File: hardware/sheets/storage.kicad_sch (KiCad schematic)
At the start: 23 parts, among them J1 Conn_02x20_Odd_Even, J2 Conn_02x25_Odd_Even, Q1 2N7002, U1 74HC04, U10 74LVC573A, U11 74HC138, U3 74HC08, U4 74HC32, U6 74HC138, U7 74HC138, U8 74LVC245A, U9 74LVC573A

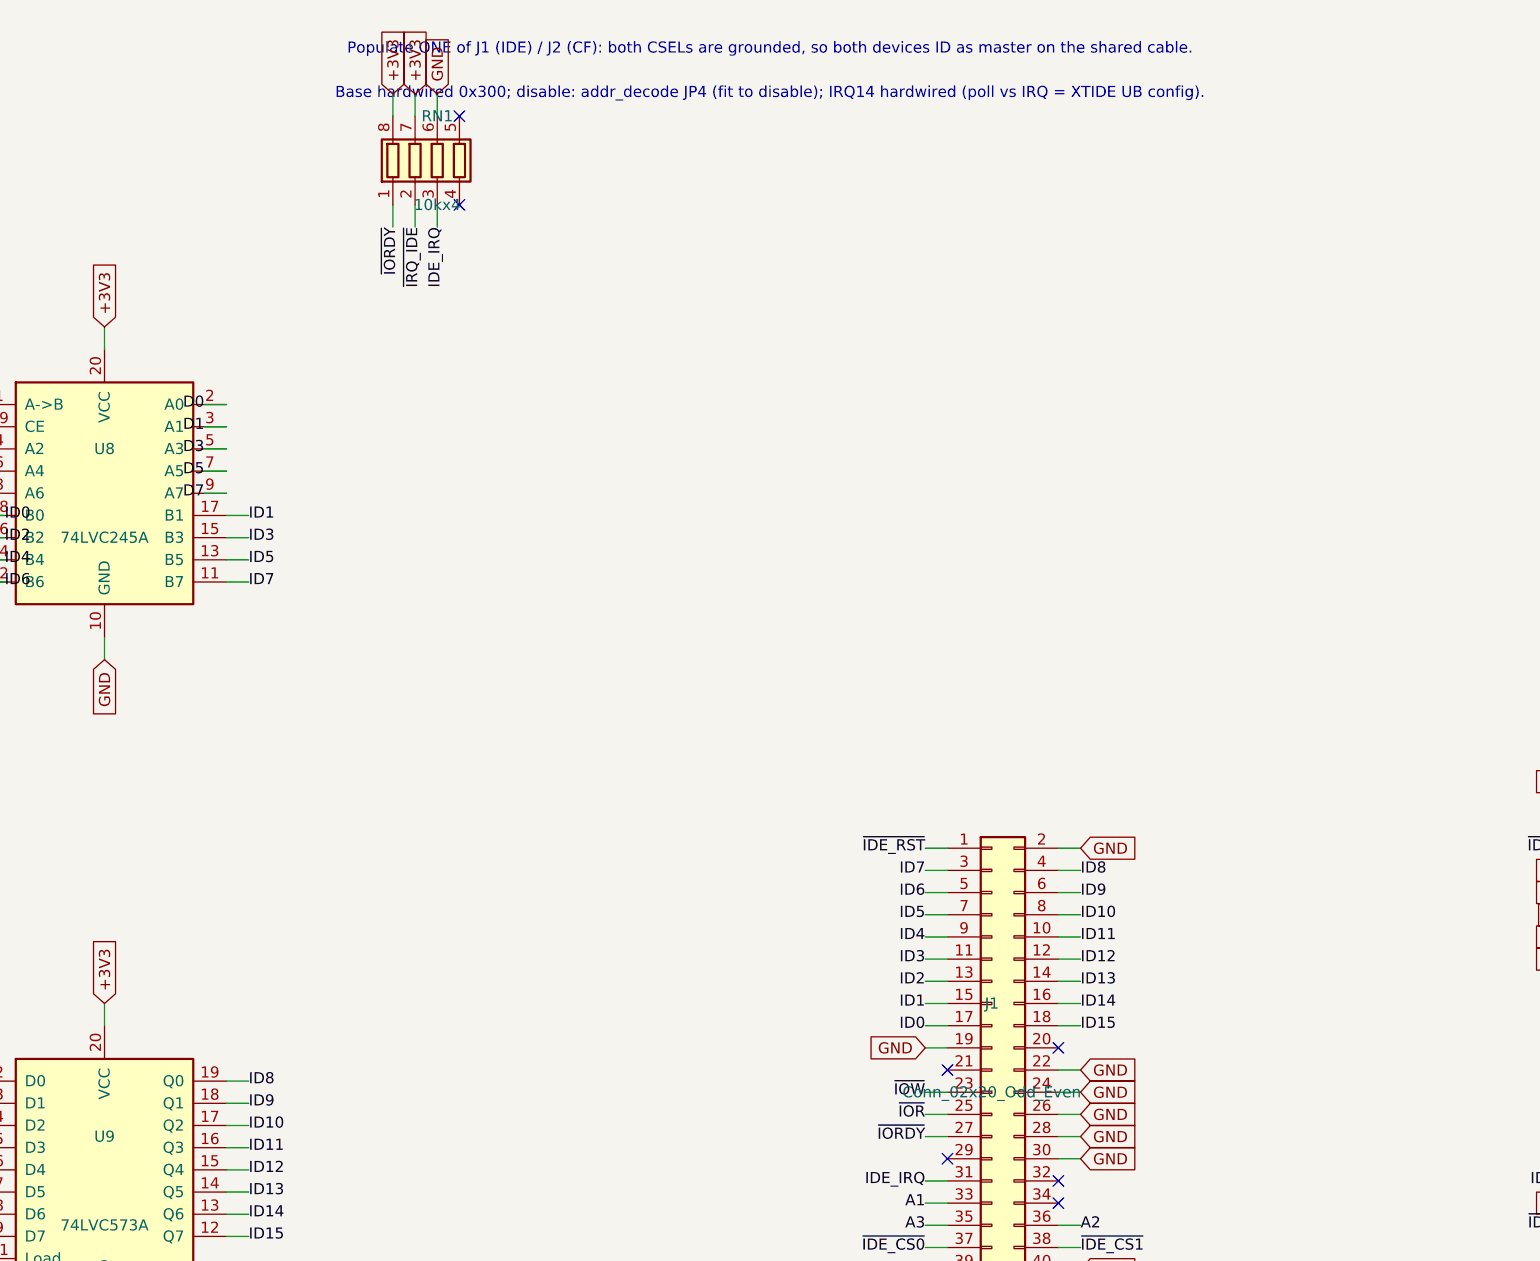
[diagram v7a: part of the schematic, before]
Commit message: Expansion port: 50-pin header, port DMA channel, dev cards deleted
Two waves of the 2026-07-14/15 expansion-port rework (the first was
uncommitted): the IRQ-scan collapse to one '165 + '32 OR rank with
ISA-card DMA removed outright, then the port redesign that brings one
DMA channel back:

- isa_conn: 60-pin (2x30, PicoGUS-standard layout) -> 50-pin (2x25,
  project-private pinout; 50-way IDC is far easier to source). OSC and
  ~REFRESH dropped to fit (no on-board consumer / no DRAM refresh; the
  planned ISA backplane board re-creates both for period cards).
- Port DMA: EXT_DRQ rides the sidecar inbound '244 + U12 '165 spare D6
  lane (zero GPIO); ~EXT_DACK = GPIO47 (freed by ~REFRESH) out through
  the strobe '244. Separate nets from the internal PicoGUS pair, so a
  port card never sees the on-board acknowledge.
- DRQ1/~DACK1 renamed DRQ/~DACK (ch2/3 long retired); DRQ2/3 +
  ~DACK2/3 removed from the mxbus contract.
- card_video + card_isatest deleted (sheets, hardware/cards/,
  build_cards()); superseded by the backplane plan. History has them.
- Connector parts: IDE header -> shrouded 2x20 IDC box (C9138, keypin
  20 NC'd); expansion port -> 90-degree 2x25 female socket (C21262364);
  addr_decode's five disable jumpers folded into ONE fixed 2x5 block
  JP1 (C492422), positions JP1.1-JP1.5 = COM1/COM2/LPT/IDE/VID.

ERC 0/0, check_parts 0 problems; docs/notes updated throughout.

Co-Authored-By: Claude Fable 5 <noreply@anthropic.com>
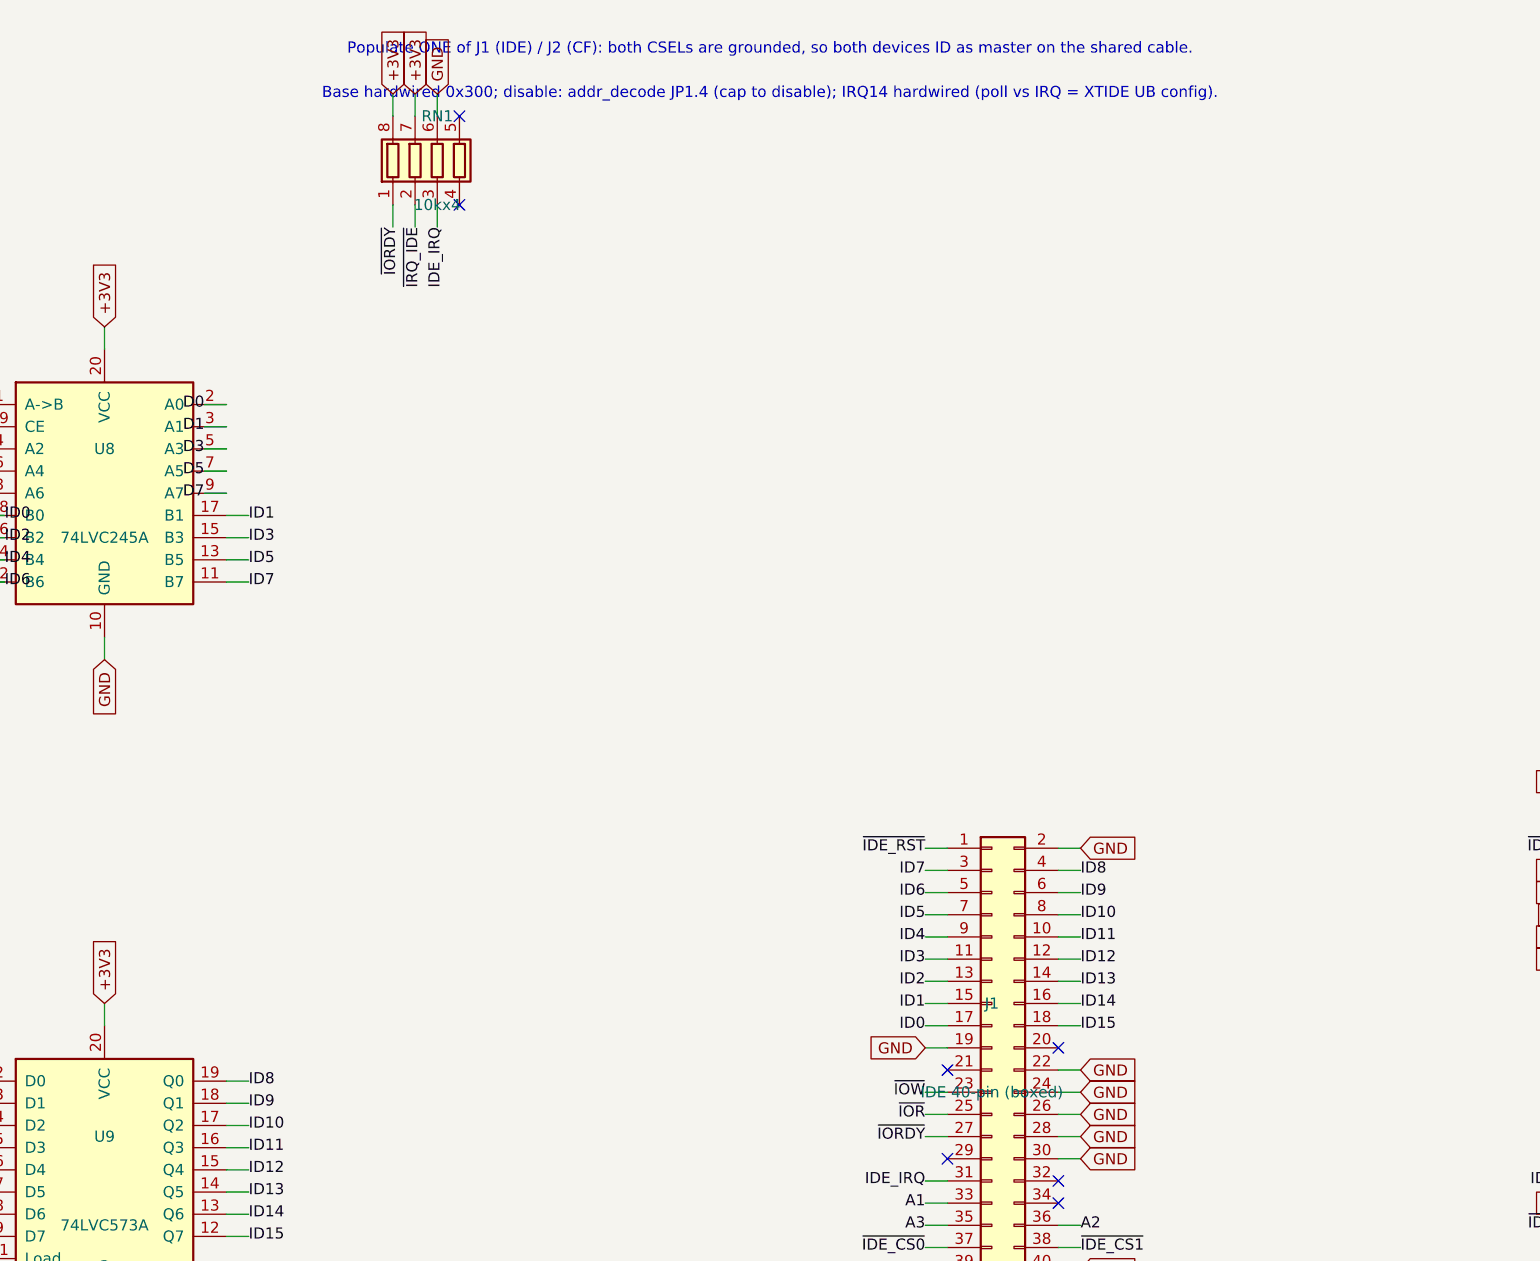
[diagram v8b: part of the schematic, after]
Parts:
- J1: value Conn_02x20_Odd_Even -> IDE 40-pin (boxed); footprint Connector_PinHeader_2.54mm:PinHeader_2x20_P2.54mm_Vertical -> Connector_IDC:IDC-Header_2x20_P2.54mm_Vertical; LCSC Part Num C2333 -> C9138
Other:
- note added: "Base hardwired 0x300; disable: addr_decode JP1.4 (cap to disable); IRQ14 hardwired (poll vs IRQ = XTIDE UB config)."
- note removed: "Base hardwired 0x300; disable: addr_decode JP4 (fit to disable); IRQ14 hardwired (poll vs IRQ = XTIDE UB config)."
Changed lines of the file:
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@@
 		)
 	)
-	(text "Base hardwired 0x300; disable: addr_decode JP4 (fit to disable); IRQ14 hardwired (poll vs IRQ = XTIDE UB config)."
+	(text "Base hardwired 0x300; disable: addr_decode JP1.4 (cap to disable); IRQ14 hardwired (poll vs IRQ = XTIDE UB config)."
 		(at 266.7 17.78 0)
 		(effects
@@
 		(instances
 			(project "mini-xt"
-				(path "/26736c46-8b40-5460-874f-03596d17270c/972bbf88-a469-5cda-af99-5a47d228ddba"
+				(path "/26736c46-8b40-5460-874f-03596d17270c/cea63665-b003-57d2-b8d8-5d97642a4726"
 					(reference "U801")
 					(unit 1)
@@
 		(instances
 			(project "mini-xt"
-				(path "/26736c46-8b40-5460-874f-03596d17270c/972bbf88-a469-5cda-af99-5a47d228ddba"
+				(path "/26736c46-8b40-5460-874f-03596d17270c/cea63665-b003-57d2-b8d8-5d97642a4726"
 					(reference "U803")
 					(unit 1)
@@
 		(instances
 			(project "mini-xt"
-				(path "/26736c46-8b40-5460-874f-03596d17270c/972bbf88-a469-5cda-af99-5a47d228ddba"
+				(path "/26736c46-8b40-5460-874f-03596d17270c/cea63665-b003-57d2-b8d8-5d97642a4726"
 					(reference "U804")
 					(unit 1)
@@
 		(instances
 			(project "mini-xt"
-				(path "/26736c46-8b40-5460-874f-03596d17270c/972bbf88-a469-5cda-af99-5a47d228ddba"
+				(path "/26736c46-8b40-5460-874f-03596d17270c/cea63665-b003-57d2-b8d8-5d97642a4726"
 					(reference "Q801")
 					(unit 1)
@@
 		(instances
 			(project "mini-xt"
-				(path "/26736c46-8b40-5460-874f-03596d17270c/972bbf88-a469-5cda-af99-5a47d228ddba"
+				(path "/26736c46-8b40-5460-874f-03596d17270c/cea63665-b003-57d2-b8d8-5d97642a4726"
 					(reference "U806")
 					(unit 1)
@@
 		(instances
 			(project "mini-xt"
-				(path "/26736c46-8b40-5460-874f-03596d17270c/972bbf88-a469-5cda-af99-5a47d228ddba"
+				(path "/26736c46-8b40-5460-874f-03596d17270c/cea63665-b003-57d2-b8d8-5d97642a4726"
 					(reference "U807")
 					(unit 1)
@@
 		(instances
 			(project "mini-xt"
-				(path "/26736c46-8b40-5460-874f-03596d17270c/972bbf88-a469-5cda-af99-5a47d228ddba"
+				(path "/26736c46-8b40-5460-874f-03596d17270c/cea63665-b003-57d2-b8d8-5d97642a4726"
 					(reference "U811")
 					(unit 1)
@@
 		(instances
 			(project "mini-xt"
-				(path "/26736c46-8b40-5460-874f-03596d17270c/972bbf88-a469-5cda-af99-5a47d228ddba"
+				(path "/26736c46-8b40-5460-874f-03596d17270c/cea63665-b003-57d2-b8d8-5d97642a4726"
 					(reference "U808")
 					(unit 1)
@@
 		(instances
 			(project "mini-xt"
-				(path "/26736c46-8b40-5460-874f-03596d17270c/972bbf88-a469-5cda-af99-5a47d228ddba"
+				(path "/26736c46-8b40-5460-874f-03596d17270c/cea63665-b003-57d2-b8d8-5d97642a4726"
 					(reference "U809")
 					(unit 1)
@@
 		(instances
 			(project "mini-xt"
-				(path "/26736c46-8b40-5460-874f-03596d17270c/972bbf88-a469-5cda-af99-5a47d228ddba"
+				(path "/26736c46-8b40-5460-874f-03596d17270c/cea63665-b003-57d2-b8d8-5d97642a4726"
 					(reference "U810")
 					(unit 1)
@@
 			)
 		)
-		(property "Value" "Conn_02x20_Odd_Even"
+		(property "Value" "IDE 40-pin (boxed)"
 			(at 292.1 132.08 0)
 			(effects
@@
 			)
 		)
-		(property "Footprint" "Connector_PinHeader_2.54mm:PinHeader_2x20_P2.54mm_Vertical"
+		(property "Footprint" "Connector_IDC:IDC-Header_2x20_P2.54mm_Vertical"
 			(at 292.1 127 0)
 			(effects
@@
 			)
 		)
-		(property "LCSC Part Num" "C2333"
+		(property "LCSC Part Num" "C9138"
 			(at 292.1 127 0)
 			(effects
@@
 		(instances
 			(project "mini-xt"
-				(path "/26736c46-8b40-5460-874f-03596d17270c/972bbf88-a469-5cda-af99-5a47d228ddba"
+				(path "/26736c46-8b40-5460-874f-03596d17270c/cea63665-b003-57d2-b8d8-5d97642a4726"
 					(reference "J801")
 					(unit 1)
@@
 		(instances
 			(project "mini-xt"
-				(path "/26736c46-8b40-5460-874f-03596d17270c/972bbf88-a469-5cda-af99-5a47d228ddba"
+				(path "/26736c46-8b40-5460-874f-03596d17270c/cea63665-b003-57d2-b8d8-5d97642a4726"
 					(reference "J802")
 					(unit 1)
@@
 		(instances
 			(project "mini-xt"
-				(path "/26736c46-8b40-5460-874f-03596d17270c/972bbf88-a469-5cda-af99-5a47d228ddba"
+				(path "/26736c46-8b40-5460-874f-03596d17270c/cea63665-b003-57d2-b8d8-5d97642a4726"
 					(reference "RN801")
 					(unit 1)
@@
 		(instances
 			(project "mini-xt"
-				(path "/26736c46-8b40-5460-874f-03596d17270c/972bbf88-a469-5cda-af99-5a47d228ddba"
+				(path "/26736c46-8b40-5460-874f-03596d17270c/cea63665-b003-57d2-b8d8-5d97642a4726"
 					(reference "C801")
 					(unit 1)
@@
 		(instances
 			(project "mini-xt"
-				(path "/26736c46-8b40-5460-874f-03596d17270c/972bbf88-a469-5cda-af99-5a47d228ddba"
+				(path "/26736c46-8b40-5460-874f-03596d17270c/cea63665-b003-57d2-b8d8-5d97642a4726"
 					(reference "C802")
 					(unit 1)
@@
 		(instances
 			(project "mini-xt"
-				(path "/26736c46-8b40-5460-874f-03596d17270c/972bbf88-a469-5cda-af99-5a47d228ddba"
+				(path "/26736c46-8b40-5460-874f-03596d17270c/cea63665-b003-57d2-b8d8-5d97642a4726"
 					(reference "C803")
 					(unit 1)
@@
 		(instances
 			(project "mini-xt"
-				(path "/26736c46-8b40-5460-874f-03596d17270c/972bbf88-a469-5cda-af99-5a47d228ddba"
+				(path "/26736c46-8b40-5460-874f-03596d17270c/cea63665-b003-57d2-b8d8-5d97642a4726"
 					(reference "C804")
 					(unit 1)
@@
 		(instances
 			(project "mini-xt"
-				(path "/26736c46-8b40-5460-874f-03596d17270c/972bbf88-a469-5cda-af99-5a47d228ddba"
+				(path "/26736c46-8b40-5460-874f-03596d17270c/cea63665-b003-57d2-b8d8-5d97642a4726"
 					(reference "C805")
 					(unit 1)
@@
 		(instances
 			(project "mini-xt"
-				(path "/26736c46-8b40-5460-874f-03596d17270c/972bbf88-a469-5cda-af99-5a47d228ddba"
+				(path "/26736c46-8b40-5460-874f-03596d17270c/cea63665-b003-57d2-b8d8-5d97642a4726"
 					(reference "C806")
 					(unit 1)
@@
 		(instances
 			(project "mini-xt"
-				(path "/26736c46-8b40-5460-874f-03596d17270c/972bbf88-a469-5cda-af99-5a47d228ddba"
+				(path "/26736c46-8b40-5460-874f-03596d17270c/cea63665-b003-57d2-b8d8-5d97642a4726"
 					(reference "C807")
 					(unit 1)
@@
 		(instances
 			(project "mini-xt"
-				(path "/26736c46-8b40-5460-874f-03596d17270c/972bbf88-a469-5cda-af99-5a47d228ddba"
+				(path "/26736c46-8b40-5460-874f-03596d17270c/cea63665-b003-57d2-b8d8-5d97642a4726"
 					(reference "C808")
 					(unit 1)
@@
 		(instances
 			(project "mini-xt"
-				(path "/26736c46-8b40-5460-874f-03596d17270c/972bbf88-a469-5cda-af99-5a47d228ddba"
+				(path "/26736c46-8b40-5460-874f-03596d17270c/cea63665-b003-57d2-b8d8-5d97642a4726"
 					(reference "C809")
 					(unit 1)
@@
 		(instances
 			(project "mini-xt"
-				(path "/26736c46-8b40-5460-874f-03596d17270c/972bbf88-a469-5cda-af99-5a47d228ddba"
+				(path "/26736c46-8b40-5460-874f-03596d17270c/cea63665-b003-57d2-b8d8-5d97642a4726"
 					(reference "C812")
 					(unit 1)
